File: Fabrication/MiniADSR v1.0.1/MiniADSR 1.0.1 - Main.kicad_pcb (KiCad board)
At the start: 2 copper layers, 20 x 102.5 mm, 31 parts, among them J3 JST_BUS, J5 IDC_BUS, J6 MainBoard_Pins, Q1 BC547, Q2 BC547, Q3 BC547, U1 LM555xN, U2 TL072

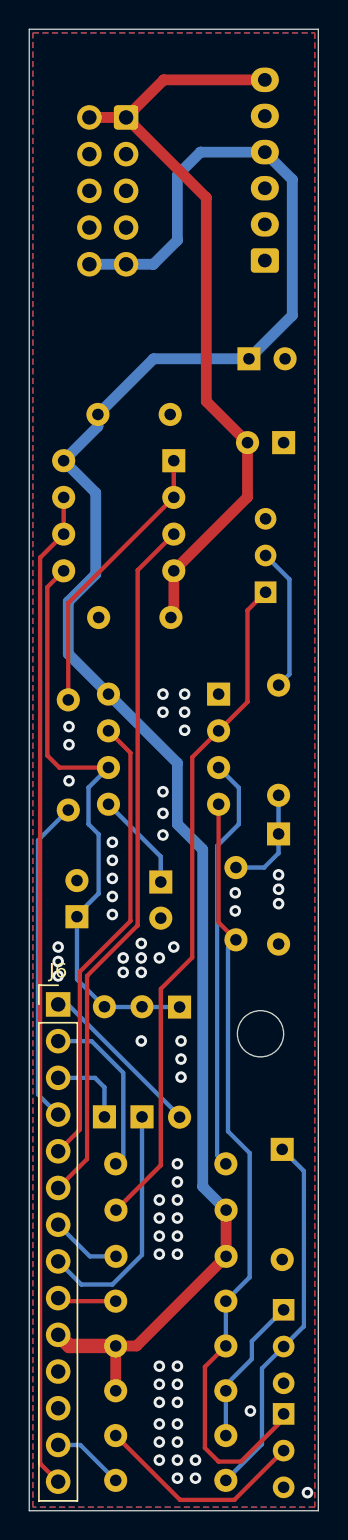
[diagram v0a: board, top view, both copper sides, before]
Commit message: Flipped power connectors for v1.0.1
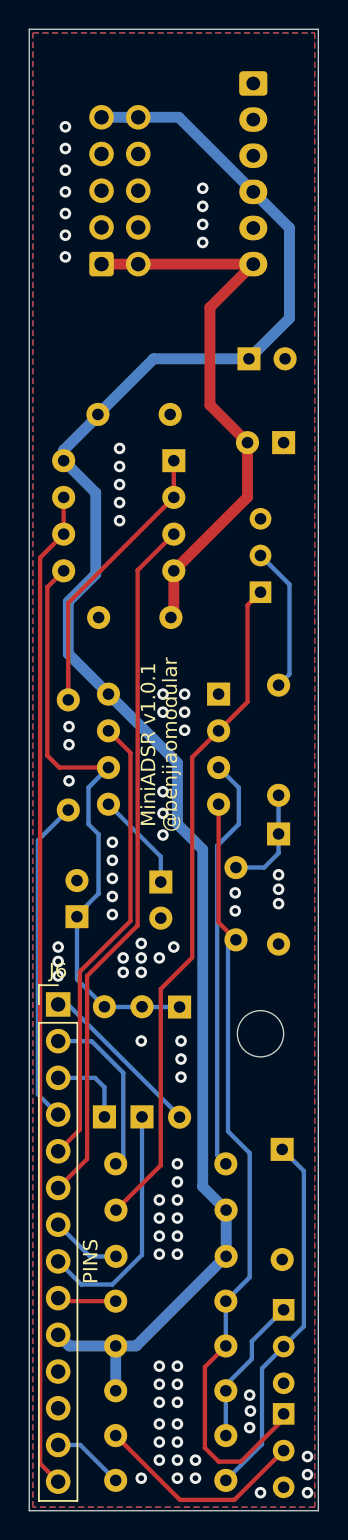
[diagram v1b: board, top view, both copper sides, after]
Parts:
- moved J3 12.3 mm to (150.5, 56.8), turned to 270 degrees
- moved J5 10.3 mm to (140.0, 69.2), turned to 0 degrees
- moved Q3 0.35 mm to (151.0, 92.0)
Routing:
- net -12V: track 53.5 -> 39.5 mm
- net +12V: track 129.4 -> 121.5 mm
- net GND2: vias 58 -> 80
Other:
- board text added: "@benjiaomodular"
- board text added: "PINS"
